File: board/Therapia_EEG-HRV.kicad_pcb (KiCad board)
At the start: 4 copper layers, 61.8 x 45 mm, 141 parts, among them J1 USB-C_16P, J2 Header_2x6

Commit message: S9: cart substitutions D_LED C84268, F1 C43379 -> parts table/BOM regenerated; Gerber unchanged
Co-Authored-By: Claude Fable 5 <noreply@anthropic.com>
Claude-Session: https://claude.ai/code/session_01431Pn2abKuPv9KnYCZmkiJ
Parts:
- D_LED: value LED red 0603 Vf1.95V -> LED yellow 0603 Vf1.6-2.6V
- F1: value PTC_500mA -> PTC 0.5A hold / 1A trip / 13.2V 1206
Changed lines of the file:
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@@
 			)
 		)
-		(property "Value" "PTC_500mA"
+		(property "Value" "PTC 0.5A hold / 1A trip / 13.2V 1206"
 			(at 0 0 90)
 			(layer "F.Fab")
@@
 			)
 		)
-		(property "MPN" "JK-NSMD050-13.2V"
-			(at 0 0 0)
-			(layer "Cmts.User")
-			(hide yes)
-			(effects
-				(font
-					(size 1.27 1.27)
-					(thickness 0.15)
-				)
-			)
-		)
-		(property "LCSC" "C369159"
+		(property "MPN" "SMD1206P050TF/13.2"
+			(at 0 0 0)
+			(layer "Cmts.User")
+			(hide yes)
+			(effects
+				(font
+					(size 1.27 1.27)
+					(thickness 0.15)
+				)
+			)
+		)
+		(property "LCSC" "C43379"
 			(at 0 0 0)
 			(layer "Cmts.User")
@@
 			)
 		)
-		(property "Value" "LED red 0603 Vf1.95V"
+		(property "Value" "LED yellow 0603 Vf1.6-2.6V"
 			(at 0 0 0)
 			(layer "F.Fab")
@@
 			)
 		)
-		(property "MPN" "19-217/R6C-AL1M2VY/3T"
-			(at 0 0 0)
-			(layer "Cmts.User")
-			(hide yes)
-			(effects
-				(font
-					(size 1.27 1.27)
-					(thickness 0.15)
-				)
-			)
-		)
-		(property "LCSC" "C72044"
-			(at 0 0 0)
-			(layer "Cmts.User")
+		(property "MPN" "NCD0603Y1"
+			(at 0 0 0)
+			(layer "Cmts.User")
+			(hide yes)
+			(effects
+				(font
+					(size 1.27 1.27)
+					(thickness 0.15)
+				)
+			)
+		)
+		(property "LCSC" "C84268"
+			(at 0 0 0)
+			(layer "Cmts.User")

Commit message: S5_L7: R_CC1 was inside the USB-C shell — moved out, rewired, and a check added so it cannot happen again
R_CC1 (0603, 5.1k CC1 pull-down) sat at (178.166, 109.464) rot 90, body
177.7405..178.6214 x 108.6385..110.3194 — 3.16 mm inside J1's F.Fab outline.
J1's shell lands flat on the board, so the connector could not have seated.
The cart was already filled; nothing in the pipeline said a word.

L7 (scripts/36_repair_L7_rcc1.py, gates/S5_L7.json)
  R_CC1 -> (173.400, 113.900) rot 180, 1.206 mm clear of J1's body, beside
  R_CC2 where the CC network belongs. No courtyard overlap; worst
  pad-to-copper gap 0.3785 mm against the 0.0889 mm rule.
  Removed: 7 USB_CC1 F.Cu tracks (the whole net — it has only J1.4 and
  R_CC1.1) and R_CC1's private ground stub, one F.Cu track plus its via at
  (178.166, 107.432), confirmed private by route.trace_island.
  Laid: USB_CC1 4.141 mm in 3 segments — F.Cu to a via at (174.879, 114.173),
  B.Cu under J1's pad column to a via at (176.5935, 112.268), F.Cu into pad 4
  from the east; GND 0.508 mm of F.Cu to a via at (172.6465, 114.408).
  Byte-identical on a second run.

  Not the brief's (173.44, 112.00): that point is on the GND track/via and the
  USB_VBUS_RAW climb. Not an F.Cu-only connection either — J1 pad 4 cannot be
  entered from the west at all: 0.2002 mm to pads 3 and 5, 0.1738 mm to the
  USB_DM via, against a 0.2667 mm minimum corridor (0.0889 track + 2 x 0.0889).
  Not the via-neutral position south of the connector: measured on the board,
  its route leaves a 0.103 mm web at J1 pad 13 and the CHASSIS_GND pour breaks
  from 2 filled islands into 4, with DRC reporting the shell leg unconnected.

lib/maze.py — a defect the repair walked into
  The open-node cache was keyed on (ix, iy, layer) with no width, so
  _via_open inherited the answer given for a 0.2032 mm track when asking about
  a 0.6095 mm via. It placed a via 0.1930 mm from J1 pad 3 — legal for the
  track, a short for the via — and in the other direction pois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
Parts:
- moved R_CC1 6.51 mm to (173.4, 113.9), turned to 180 degrees
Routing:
- net USB_CC1: track 5.04 -> 4.14 mm, vias 0 -> 2
- net GND: track 84.9 -> 84.1 mm
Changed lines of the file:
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@@
 	(footprint "ProPrj_The-easyedapro:R0603"
 		(layer "F.Cu")
-		(at 178.166 109.464 90)
+		(at 173.4 113.9 180)
 		(property "Reference" "R_CC1"
-			(at -1.4615 -0.864 90)
+			(at -1.4615 -0.864 180)
 			(layer "F.SilkS")
 			(hide yes)
@@
 		)
 		(property "Value" "5.1k"
-			(at 0 0 90)
+			(at 0 0 180)
 			(layer "F.Fab")
 			(effects
@@
 		)
 		(property "Datasheet" ""
-			(at 0 0 90)
+			(at 0 0 180)
 			(layer "F.Fab")
 			(hide yes)
@@
 		)
 		(property "Description" ""
-			(at 0 0 90)
+			(at 0 0 180)
 			(layer "F.Fab")
 			(hide yes)
@@
 		)
 		(property "JLC_3DModel_Q" "112863783b5b41f1b5254f87eedc7932"
-			(at 0 0 90)
+			(at 0 0 180)
 			(layer "Cmts.User")
 			(hide yes)
@@
 		)
 		(property "JLC_3D_Size" "0.81 1.62"
-			(at 0 0 90)
+			(at 0 0 180)
 			(layer "Cmts.User")
 			(hide yes)
@@
 		)
 		(property "MPN" "0603WAF5101T5E"
-			(at 0 0 0)
+			(at 0 0 90)
 			(layer "Cmts.User")
 			(hide yes)
@@
 		)
 		(property "LCSC" "C23186"
-			(at 0 0 0)
+			(at 0 0 90)
 			(layer "Cmts.User")
 			(hide yes)
@@
 		(duplicate_pad_numbers_are_jumpers no)
 		(fp_line
-			(start 1.385 -0.6605)
-			(end 0.426 -0.6605)
+			(start 1.385 0.6605)
+			(end 1.385 -0.6605)
 			(stroke
 				(width 0.1525)
@@
 		)
 		(fp_line
-			(start -1.385 -0.6605)
-			(end -0.426 -0.6605)
+			(start 1.385 -0.6605)
+			(end 0.426 -0.6605)
 			(stroke
 				(width 0.1525)
@@
 		)
 		(fp_line
-			(start 1.385 0.6605)
-			(end 1.385 -0.6605)
+			(start 0.426 0.6605)
+			(end 1.385 0.6605)
 			(stroke
 				(width 0.1525)
@@
 		)
 		(fp_line
-			(start 0.426 0.6605)
-			(end 1.385 0.6605)
+			(start -0.426 0.6605)
+			(end -1.385 0.6605)
 			(stroke
 				(width 0.1525)
@@
 		)
 		(fp_line
-			(start -0.426 0.6605)
-			(end -1.385 0.6605)
+			(start -1.385 0.6605)
+			(end -1.385 -0.6605)
 			(stroke
 				(width 0.1525)
@@
 		)
 		(fp_line
-			(start -1.385 0.6605)
-			(end -1.385 -0.6605)
+			(start -1.385 -0.6605)
+			(end -0.426 -0.6605)
 			(stroke
 				(width 0.1525)
@@
 		)
 		(fp_line
-			(start 0.8 -0.4)
-			(end 0.8 0.4)
+			(start 0.8 0.4)
+			(end -0.8 0.4)
 			(stroke
 				(width 0.051)
@@
 		)
 		(fp_line
-			(start -0.8 -0.4)
-			(end 0.8 -0.4)
+			(start 0.8 -0.4)
+			(end 0.8 0.4)
 			(stroke
 				(width 0.051)
@@
 		)
 		(fp_line
-			(start 0.8 0.4)
-			(end -0.8 0.4)
+			(start -0.8 0.4)
+			(end -0.8 -0.4)
 			(stroke
 				(width 0.051)
@@
 		)
 		(fp_line
-			(start -0.8 0.4)
-			(end -0.8 -0.4)
+			(start -0.8 -0.4)
+			(end 0.8 -0.4)
 			(stroke
 				(width 0.051)
@@
 		)
 		(fp_text user "${REFERENCE}"
-			(at 0 0 90)
+			(at 0 0 180)
 			(layer "F.Fab")
 			(effects
@@
 		)
 		(pad "1" smd rect
-			(at -0.7535 0 90)
+			(at -0.7535 0 180)
 			(size 0.8065 0.864)
 			(layers "F.Cu" "F.Mask" "F.Paste")
@@
 		)
 		(pad "2" smd rect
-			(at 0.7535 0 90)
+			(at 0.7535 0 180)
 			(size 0.8065 0.864)
 			(layers "F.Cu" "F.Mask" "F.Paste")
@@
 	)
 	(segment
-		(start 178.166 107.432)
-		(end 178.166 108.7145)
-		(width 0.203)
+		(start 172.6465 113.9)
+		(end 172.6465 114.408)
+		(width 0.2032)
 		(layer "F.Cu")
 		(net "GND")
@@
 	)
 	(via
+		(at 172.6465 114.408)
+		(size 0.6096)
+		(drill 0.3048)
+		(layers "F.Cu" "B.Cu")
+		(net "GND")
+	)
+	(via
 		(at 161.402 120.132)
 		(size 0.6095)
@@
 		(net "GND")
 	)
-	(via
-		(at 178.166 107.432)
-		(size 0.6095)
-		(drill 0.305)
-		(layers "F.Cu" "B.Cu")
-		(net "GND")
-	)
 	(segment
 		(start 144.13 122.367)
@@
 	)
 	(segment
-		(start 176.388 112.2325)
-		(end 177.0485 112.2325)
-		(width 0.203)
-		(layer "F.Cu")
-		(net "USB_CC1")
-	)
-	(segment
-		(start 177.658 111.6485)
-		(end 178.166 111.1405)
-		(width 0.203)
-		(layer "F.Cu")
-		(net "USB_CC1")
-	)
-	(segment
-		(start 178.166 111.1405)
-		(end 178.166 110.2135)
-		(width 0.203)
+		(start 176.5935 112.268)
+		(end 175.791 112.238)
+		(width 0.2032)
 		(layer "F.Cu")
 		(net "USB_CC1")
 	)
 	(segment
-		(start 175.931 112.2325)
-		(end 176.388 112.2325)
-		(width 0.203)
+		(start 174.1535 113.9)
+		(end 174.879 114.173)
+		(width 0.2032)
 		(layer "F.Cu")
 		(net "USB_CC1")
 	)
-	(segment
-		(start 177.658 111.6485)
-		(end 178.3185 111.1405)
-		(width 0.203)
-		(layer "F.Cu")
+	(via
+		(at 174.879 114.173)
+		(size 0.6096)
+		(drill 0.3048)
+		(layers "F.Cu" "B.Cu")
 		(net "USB_CC1")
 	)
-	(segment
-		(start 176.388 112.2325)
-		(end 175.791 112.2375)
-		(width 0.203)
-		(layer "F.Cu")
+	(via
+		(at 176.5935 112.268)
+		(size 0.6096)
+		(drill 0.3048)
+		(layers "F.Cu" "B.Cu")
 		(net "USB_CC1")
 	)
 	(segment
-		(start 177.0485 112.2325)
-		(end 177.658 111.6485)
-		(width 0.203)
-		(layer "F.Cu")
+		(start 174.879 114.173)
+		(end 176.5935 112.268)
+		(width 0.2032)
+		(layer "B.Cu")
 		(net "USB_CC1")
 	)

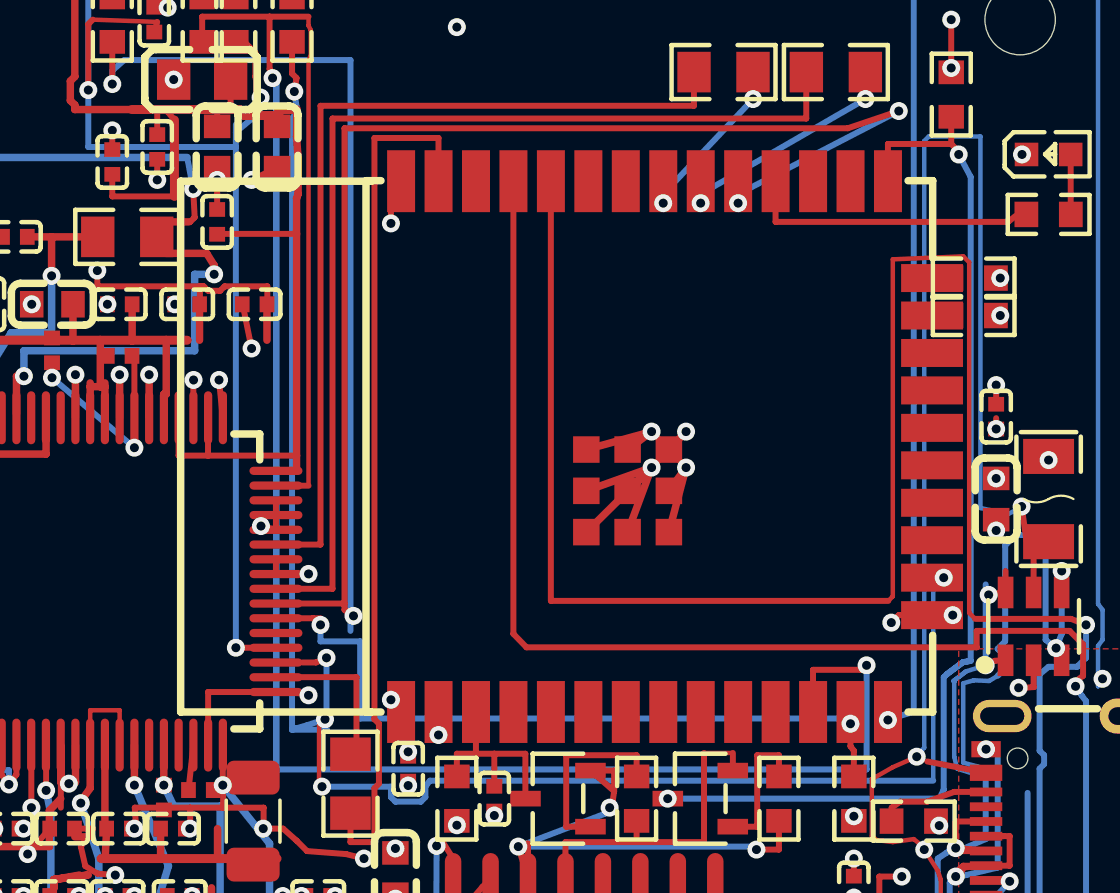
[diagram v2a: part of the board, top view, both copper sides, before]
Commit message: S5_L8: U_MCU becomes an ESP32-WROOM-32UE -- the 25.5 mm body was lying across the ADC
ACCEPTANCE H failed on four pairs and all four were the same fact: the
ESP32-WROOM-32E's outline is 25.5 mm long, 6.3 mm of it PCB antenna and
keep-out at the -X end, and that end points at the ADS1299. It reached
2.81 mm into the ADC's package and covered C_AVDD1_100n, C_AVDD1_10n and
C_DVDD_P40.

The lead's decision, recorded in data/bom_fixes_2026-08-28.json: fit the
ESP32-WROOM-32UE-N4 (C701344) instead. Espressif's datasheet says the pin
layout is identical except for the keep-out, so all 38 pads stay where they
are -- this touches no copper at all. 19.2 x 18 x 3.2 mm body, JLC stock
5,490, Extended/Standard Only, the same assembly category the cart already
assumes. Rev.A is USB-UART only, so nothing needs the antenna.

scripts/37_umcu_32ue.py redraws the outline on F.Fab (four lines), F.SilkS
(seven segments, derived from the pads so the silk cannot land on a
castellation -- they come out at the same coordinates the 32E outline used)
and F.CrtYd (body + 0.25), carries the pin-1 marker to the new corner, and
sets Value / MPN / LCSC. Idempotent.

Measured after: U_ADS 3.7701 mm (was -2.8124), C_AVDD1_10n 3.4441 (-3.1384),
C_DVDD_P40 4.9341 (-1.6484), C_AVDD1_100n 5.7301 (-0.8524). DRC 0 errors,
0 unconnected, no new signatures; contract parity 0; counts unchanged.

Co-Authored-By: Claude Fable 5 <noreply@anthropic.com>
Claude-Session: https://claude.ai/code/session_01431Pn2abKuPv9KnYCZmkiJ
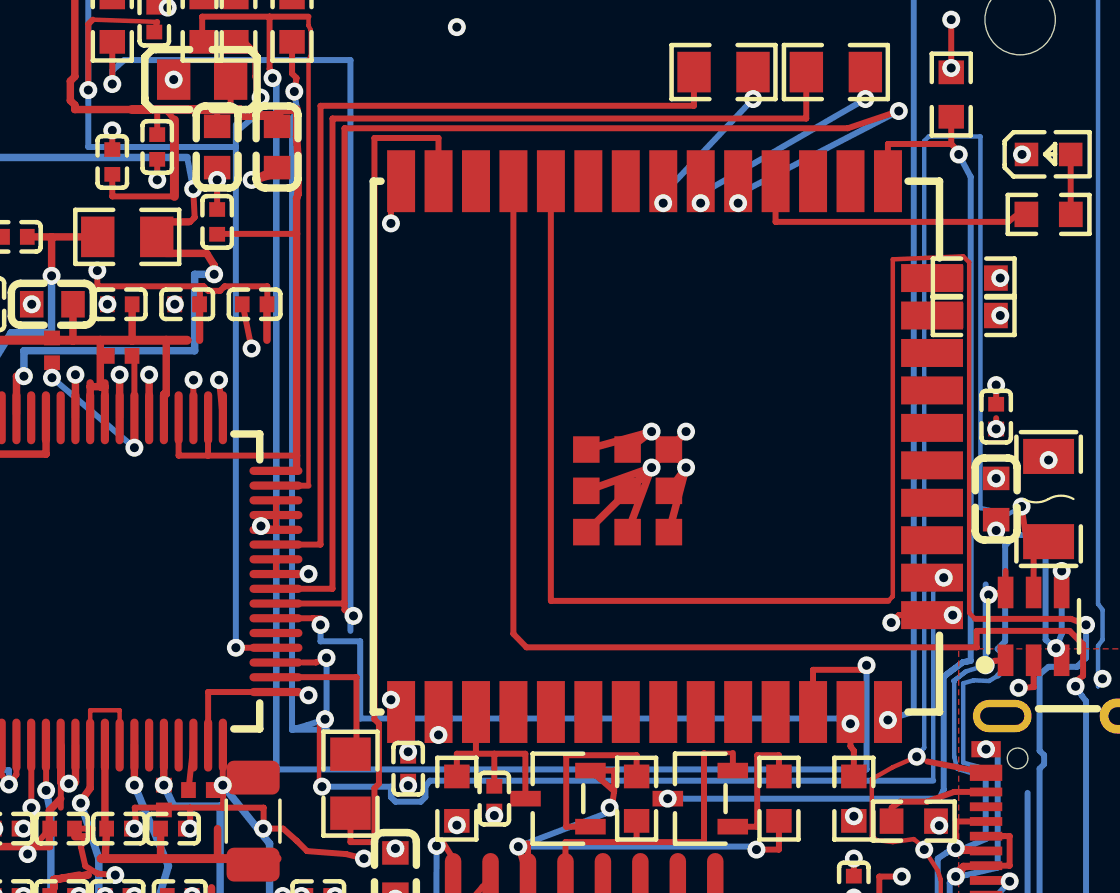
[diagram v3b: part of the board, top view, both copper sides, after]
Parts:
- U_MCU: value ESP32-WROOM-32E-N4 -> ESP32-WROOM-32UE-N4
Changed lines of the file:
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@@
 			)
 		)
-		(property "Value" "ESP32-WROOM-32E-N4"
+		(property "Value" "ESP32-WROOM-32UE-N4"
 			(at 0 0 0)
 			(layer "F.Fab")
@@
 			)
 		)
-		(property "MPN" "ESP32-WROOM-32E-N4"
-			(at 0 0 0)
-			(layer "Cmts.User")
-			(hide yes)
-			(effects
-				(font
-					(size 1.27 1.27)
-					(thickness 0.15)
-				)
-			)
-		)
-		(property "LCSC" "C701341"
+		(property "MPN" "ESP32-WROOM-32UE-N4"
+			(at 0 0 0)
+			(layer "Cmts.User")
+			(hide yes)
+			(effects
+				(font
+					(size 1.27 1.27)
+					(thickness 0.15)
+				)
+			)
+		)
+		(property "LCSC" "C701344"
 			(at 0 0 0)
 			(layer "Cmts.User")
@@
 		(duplicate_pad_numbers_are_jumpers no)
 		(fp_line
-			(start -16.4765 -9)
-			(end -16.4765 9)
-			(stroke
-				(width 0.254)
-				(type default)
-			)
-			(layer "F.SilkS")
-		)
-		(fp_line
-			(start -16.4765 -9)
-			(end -10.0105 -9)
-			(stroke
-				(width 0.254)
-				(type default)
-			)
-			(layer "F.SilkS")
-		)
-		(fp_line
-			(start -16.4765 9)
-			(end -10.0265 9)
-			(stroke
-				(width 0.254)
-				(type default)
-			)
-			(layer "F.SilkS")
-		)
-		(fp_line
-			(start -10.1925 -9)
-			(end -10.1925 9)
-			(stroke
-				(width 0.254)
-				(type default)
-			)
-			(layer "F.SilkS")
-		)
-		(fp_line
-			(start -10.1925 9)
+			(start -9.945 -9)
+			(end -9.945 9)
+			(stroke
+				(width 0.254)
+				(type default)
+			)
+			(layer "F.SilkS")
+		)
+		(fp_line
+			(start -9.945 -9)
+			(end -9.6835 -9)
+			(stroke
+				(width 0.254)
+				(type default)
+			)
+			(layer "F.SilkS")
+		)
+		(fp_line
+			(start -9.945 9)
 			(end -9.6835 9)
 			(stroke
@@
 		)
 		(fp_line
-			(start -9.6835 -9.017)
-			(end -10.1925 -9.017)
+			(start 8.1885 -9)
+			(end 9.255 -9)
 			(stroke
 				(width 0.254)
@@
 		(fp_line
 			(start 8.1885 9)
-			(end 9.0235 9)
-			(stroke
-				(width 0.254)
-				(type default)
-			)
-			(layer "F.SilkS")
-		)
-		(fp_line
-			(start 9.0235 -9.017)
-			(end 8.1885 -9.017)
-			(stroke
-				(width 0.254)
-				(type default)
-			)
-			(layer "F.SilkS")
-		)
-		(fp_line
-			(start 9.0235 -6.396)
-			(end 9.0235 -9.017)
-			(stroke
-				(width 0.254)
-				(type default)
-			)
-			(layer "F.SilkS")
-		)
-		(fp_line
-			(start 9.0235 9)
-			(end 9.0235 6.396)
+			(end 9.255 9)
+			(stroke
+				(width 0.254)
+				(type default)
+			)
+			(layer "F.SilkS")
+		)
+		(fp_line
+			(start 9.255 -9)
+			(end 9.255 -6.396)
+			(stroke
+				(width 0.254)
+				(type default)
+			)
+			(layer "F.SilkS")
+		)
+		(fp_line
+			(start 9.255 6.396)
+			(end 9.255 9)
 			(stroke
 				(width 0.254)
@@
 		)
 		(fp_rect
-			(start -16.832933 -10.3)
-			(end 10.3025 10.3)
+			(start -10.195 -9.25)
+			(end 9.505 9.25)
 			(stroke
 				(width 0.05)
@@
 		)
 		(fp_line
-			(start -16.5275 -9)
-			(end 8.9725 -9)
-			(stroke
-				(width 0.051)
-				(type default)
-			)
-			(layer "F.Fab")
-		)
-		(fp_line
-			(start -16.5275 9)
-			(end -16.5275 -9)
-			(stroke
-				(width 0.051)
-				(type default)
-			)
-			(layer "F.Fab")
-		)
-		(fp_line
-			(start 8.9725 -9)
-			(end 8.9725 9)
-			(stroke
-				(width 0.051)
-				(type default)
-			)
-			(layer "F.Fab")
-		)
-		(fp_line
-			(start 8.9725 9)
-			(end -16.5275 9)
+			(start -9.945 -9)
+			(end 9.255 -9)
+			(stroke
+				(width 0.051)
+				(type default)
+			)
+			(layer "F.Fab")
+		)
+		(fp_line
+			(start -9.945 9)
+			(end -9.945 -9)
+			(stroke
+				(width 0.051)
+				(type default)
+			)
+			(layer "F.Fab")
+		)
+		(fp_line
+			(start 9.255 -9)
+			(end 9.255 9)
+			(stroke
+				(width 0.051)
+				(type default)
+			)
+			(layer "F.Fab")
+		)
+		(fp_line
+			(start 9.255 9)
+			(end -9.945 9)
 			(stroke
 				(width 0.051)
@@
 		(fp_poly
 			(pts
-				(xy -16.472067 8.977039) (xy -16.504539 8.944567) (xy -16.550461 8.944567) (xy -16.582933 8.977039)
-				(xy -16.582933 9.022961) (xy -16.550461 9.055433) (xy -16.504539 9.055433) (xy -16.472067 9.022961)
-			)
-			(stroke
+				(xy -9.889567 8.977039) (xy -9.922039 8.944567) (xy -9.967961 8.944567) (xy -10.000433 8.977039)
+				(xy -10.000433 9.022961) (xy -9.967961 9.055433) (xy -9.922039 9.055433) (xy -9.889567 9.022961)
+			)
+			(stroke
